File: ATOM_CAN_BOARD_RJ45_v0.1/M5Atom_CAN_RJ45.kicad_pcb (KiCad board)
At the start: 2 copper layers, 43 x 46 mm, 9 parts, among them J1 RJ45, J2 RJ45, J3 Conn_01x06_Male, J4 Conn_01x02_Male, U1 MCP2562-E-P, U2 ATOM_Lite

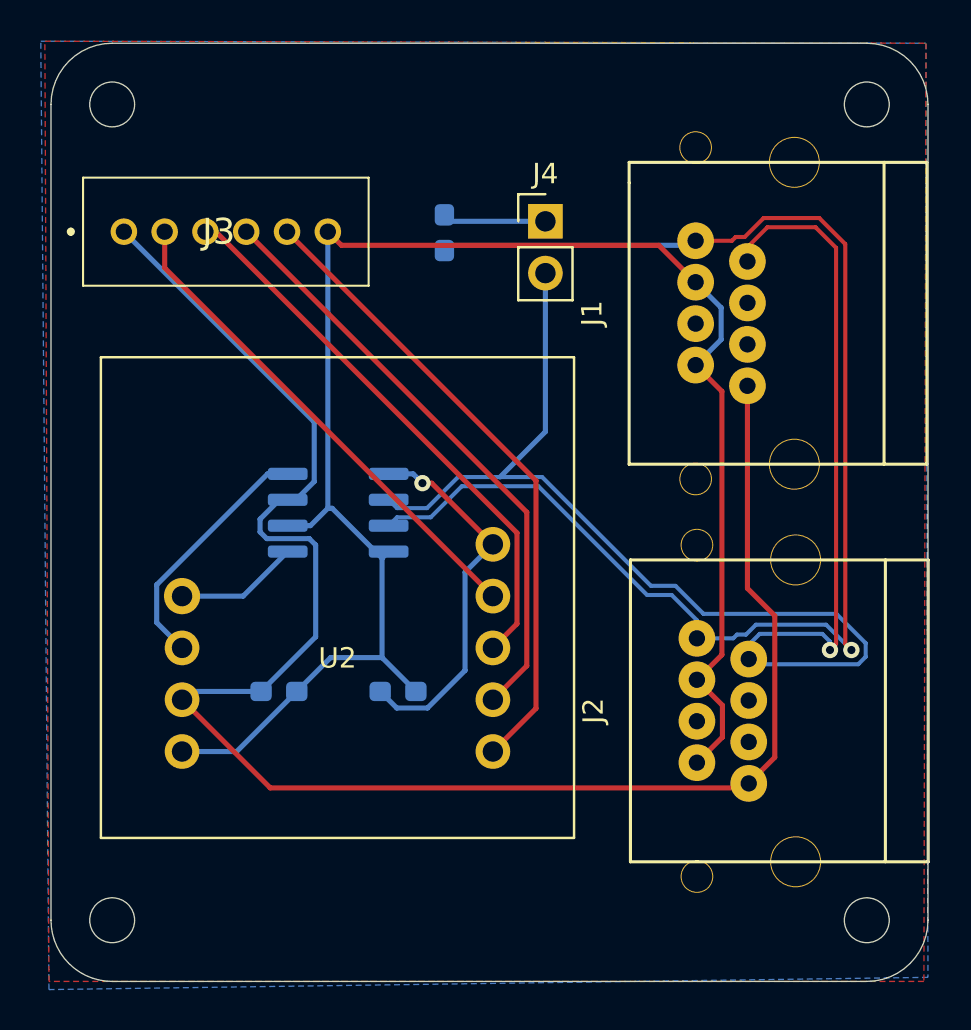
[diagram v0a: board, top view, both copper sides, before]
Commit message: ATOM_CAN_BOARD_v0.2 and RJ45_v0.1 update
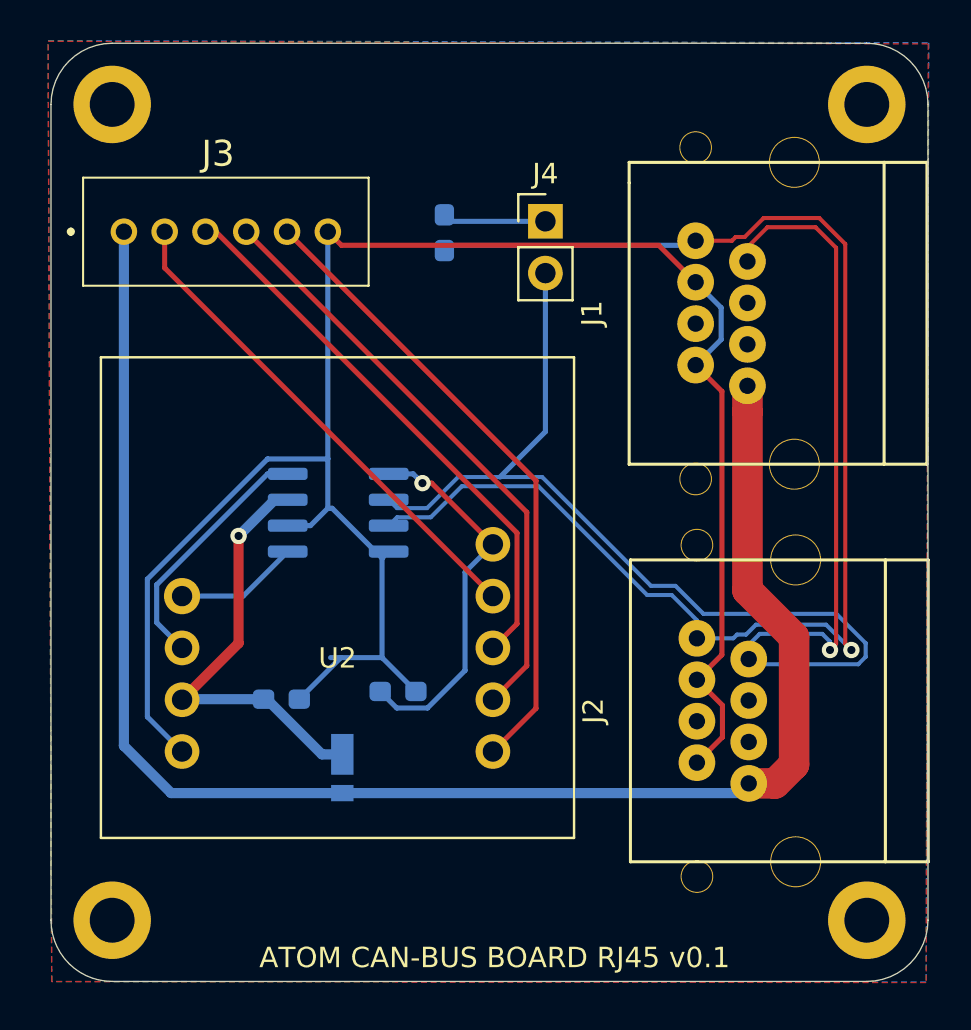
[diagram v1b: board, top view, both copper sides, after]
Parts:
- added D1: D_Schottky, Diode_SMD:D_TUMD2, B.Cu at (148.3, 113.7)
- added REF**: MountingHole_2.2mm_M2_ISO14580_Pad, MountingHole:MountingHole_2.2mm_M2_ISO14580_Pad, F.Cu at (137.0, 121.2)
- added REF**: MountingHole_2.2mm_M2_ISO14580_Pad, MountingHole:MountingHole_2.2mm_M2_ISO14580_Pad, F.Cu at (174.0, 121.2)
- added REF**: MountingHole_2.2mm_M2_ISO14580_Pad, MountingHole:MountingHole_2.2mm_M2_ISO14580_Pad, F.Cu at (174.0, 81.2)
- added REF**: MountingHole_2.2mm_M2_ISO14580_Pad, MountingHole:MountingHole_2.2mm_M2_ISO14580_Pad, F.Cu at (137.0, 81.2)
- moved C2 0.40 mm to (145.3, 110.4)
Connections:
- C2 pad 1: +5V -> Net-(C2-Pad1)
- U1 pad 3: +5V -> Net-(C2-Pad1)
- U2 pad 3: +5V -> Net-(C2-Pad1)
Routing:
- net Net-(C2-Pad1): track 0.00 -> 21.7 mm, vias 0 -> 1
- net GND: track 84.7 -> 98.8 mm
- net +5V: track 85.7 -> 79.4 mm
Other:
- outline, holes or cut-outs redrawn
- net class +5V added: clearance 0.2, trace_width 0.5, via_dia 0.8, via_drill 0.4
- board text added: "ATOM CAN-BUS BOARD RJ45 v0.1"
